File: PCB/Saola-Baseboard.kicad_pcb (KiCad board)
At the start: 2 copper layers, 54 x 54 mm, 15 parts, among them J1 USB_B_Mini, J2 UART, J3 GND, J4 3v3, J5 5v, J6 Conn_02x16_Odd_Even, J7 JTAG, J8 Conn_01x21, J9 Conn_01x21, U1 USBLC6-2SC6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

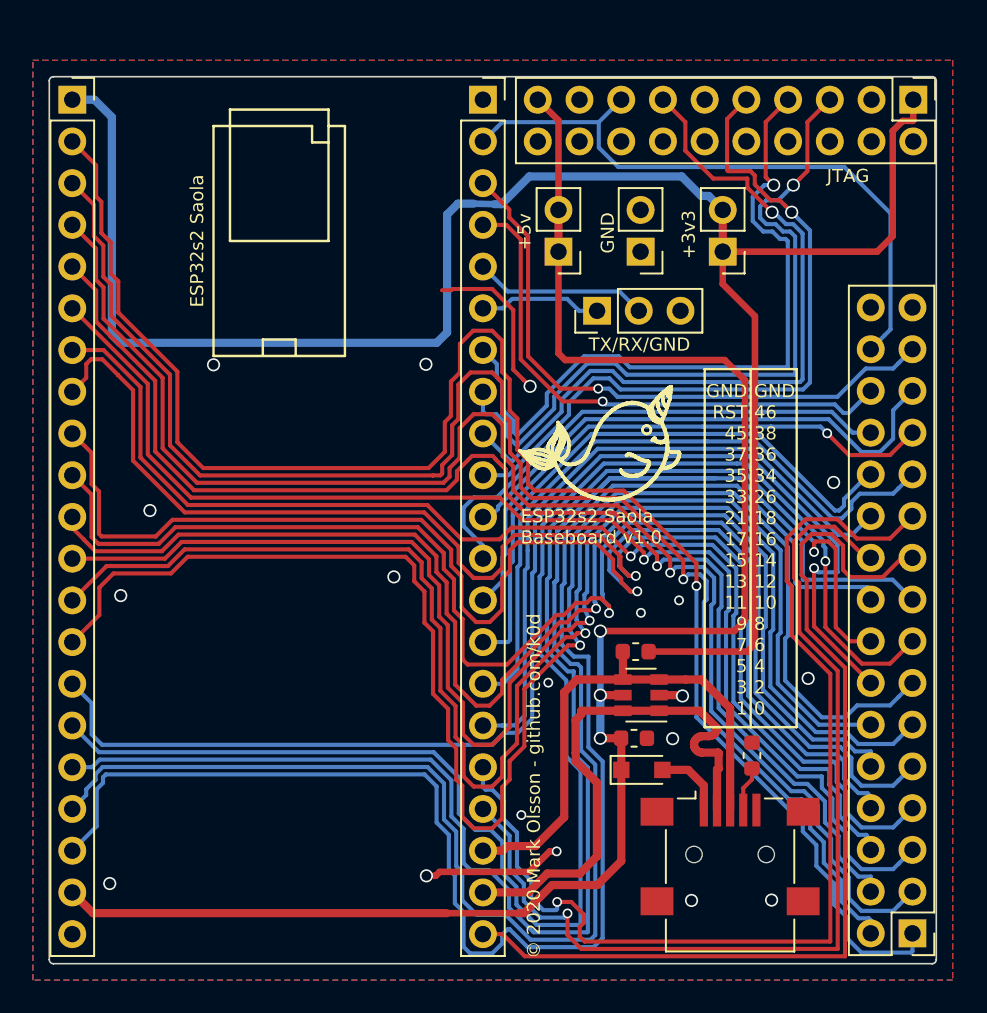
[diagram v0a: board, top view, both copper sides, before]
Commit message: Updated silkscreen
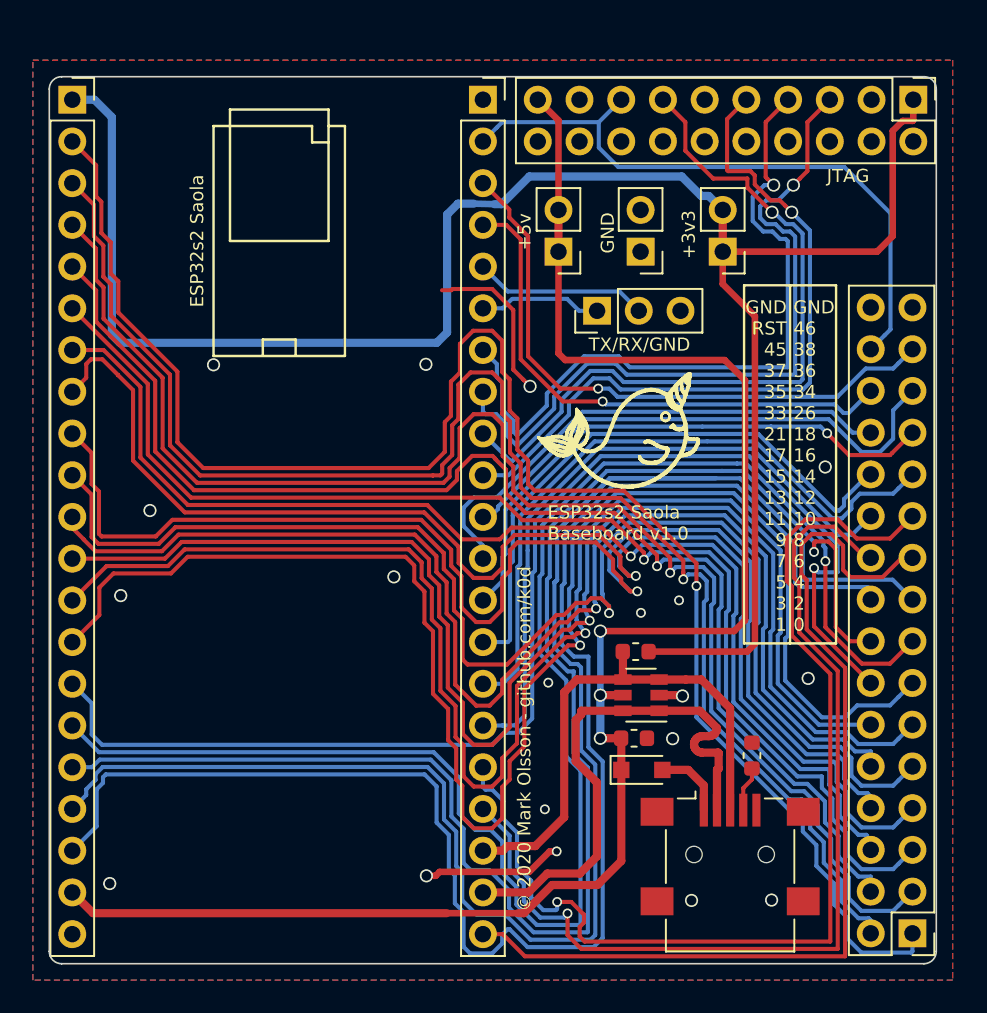
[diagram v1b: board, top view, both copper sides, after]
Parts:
- moved X1 1.39 mm to (173.1, 68.6)
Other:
- outline, holes or cut-outs redrawn

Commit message: v1.0 release
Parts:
- C1: footprint Capacitor_SMD:C_0603_1608Metric -> 01_Passives:C_0603_1608Metric
- D1: footprint Diode_SMD:D_SOD-323_HandSoldering -> 01_Passives:D_SOD-323
- J1: footprint Connector_USB:USB_Mini-B_Lumberg_2486_01_Horizontal -> 01_Connectors:USB_Mini-B_Socket
- J2: footprint Connector_PinHeader_2.54mm:PinHeader_1x03_P2.54mm_Vertical -> 01_Headers_2.54:M_1x03_2.54_V
- J3, J4, J5: footprint Connector_PinHeader_2.54mm:PinHeader_1x02_P2.54mm_Vertical -> 01_Headers_2.54:M_1x02_2.54_V
- J6: footprint Connector_PinHeader_2.54mm:PinHeader_2x16_P2.54mm_Vertical -> 01_Headers_2.54:M_2x16_2.54_V
- J7: footprint Connector_PinHeader_2.54mm:PinHeader_2x10_P2.54mm_Vertical -> 01_Headers_2.54:M_2x10_2.54_V
- J8, J9: footprint Connector_PinSocket_2.54mm:PinSocket_1x21_P2.54mm_Vertical -> 01_Headers_2.54:F_1x21_2.54_V
- R1, R2: footprint Resistor_SMD:R_0603_1608Metric -> 01_Passives:R_0603_1608Metric
- U1: footprint Package_TO_SOT_SMD:SOT-23-6 -> 01_Packages:SOT-23-6
- moved J2 5.15 mm to (176.8, 61.3), turned to 270 degrees
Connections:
- J2 pad 1: /TX -> GND
- J2 pad 3: GND -> /TX
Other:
- board text added: "."
- board text added: "JLCJLCJLCJLC"
- board text added: "TX RX GND"
- board text removed: "TX/RX/GND"
